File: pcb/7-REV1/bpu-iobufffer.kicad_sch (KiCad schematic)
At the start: 44 parts, among them J301 Conn_01x10, J302 Conn_01x09, U14 IP4220CZ6F, U15 IP4220CZ6F, U301 AiP74LVC1T45GC363.TR, U302 AiP74LVC1T45GC363.TR, U303 AiP74LVC1T45GC363.TR, U304 AiP74LVC1T45GC363.TR, U305 AiP74LVC1T45GC363.TR, U306 AiP74LVC1T45GC363.TR, U307 AiP74LVC1T45GC363.TR, U308 AiP74LVC1T45GC363.TR

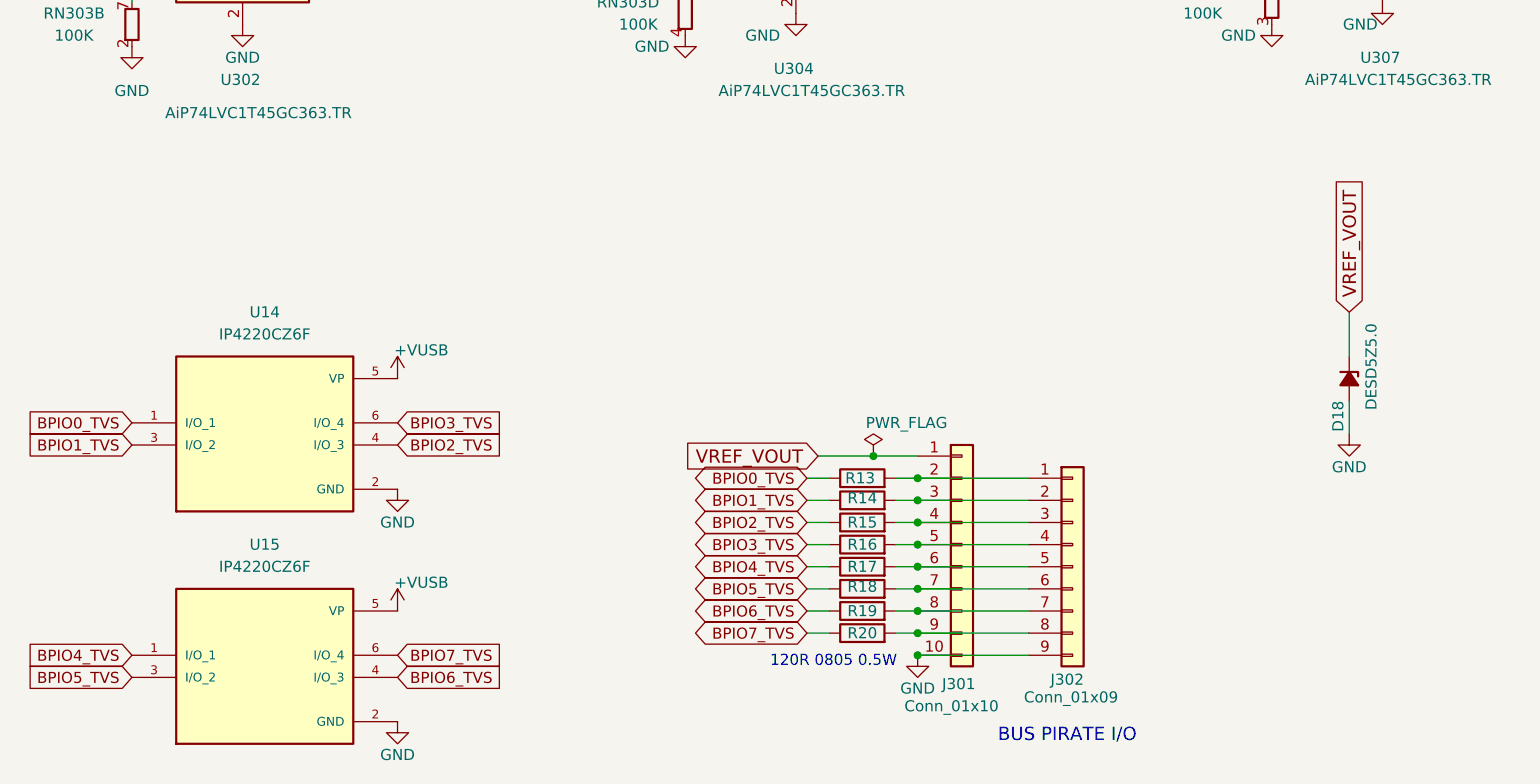
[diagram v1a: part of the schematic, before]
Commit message: adapt the IO-port protection
- move to the bpu-iobuffer sheet, remove duplicate on VOUT-protection
- use SP3002-04JTG in SOT363 instead of the larger IP4220CZ6F
- add datasheet, resistor wattage to part fields
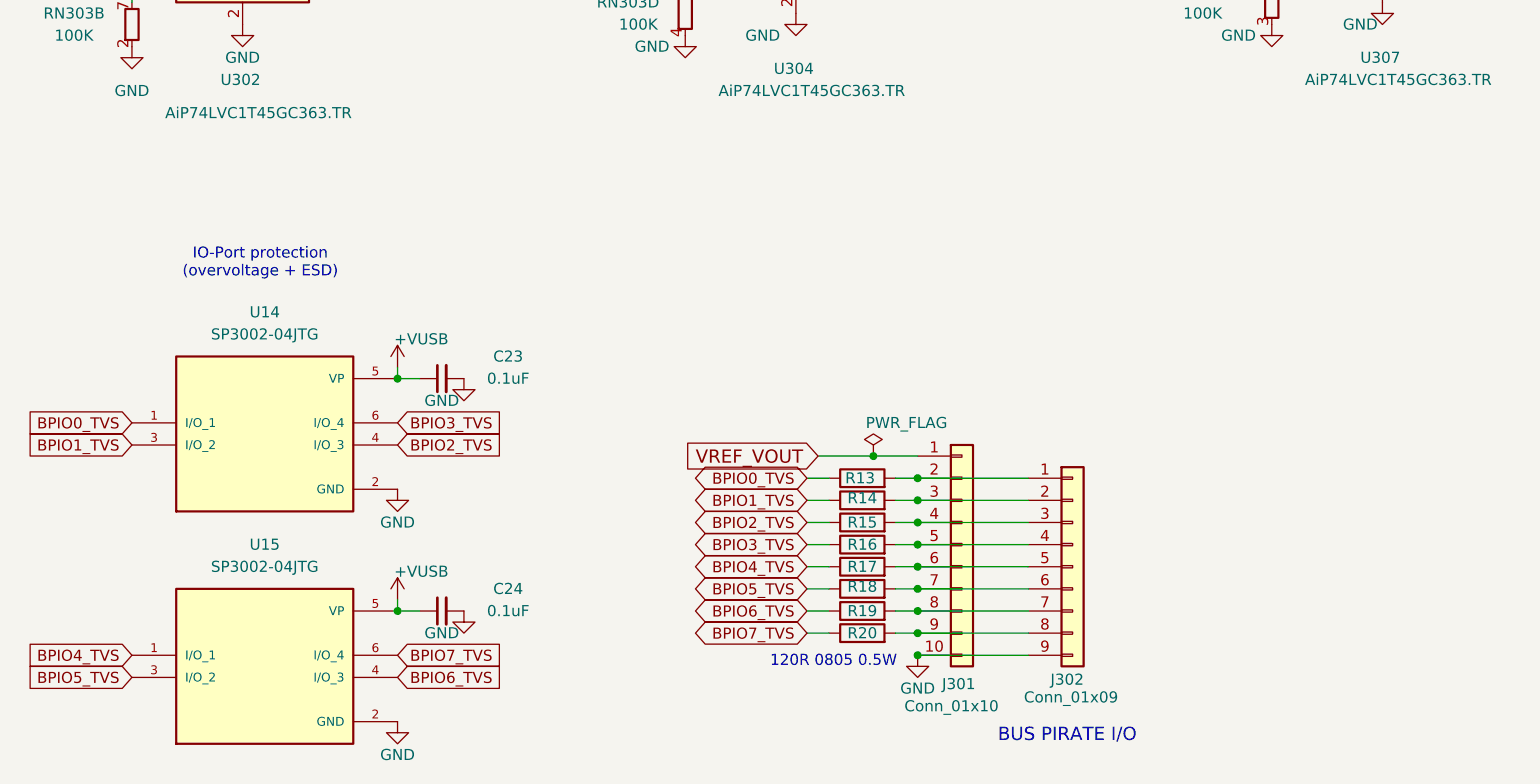
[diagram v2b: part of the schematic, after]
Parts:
- removed D18: DESD5Z5.0, Diode_SMD:D_SOD-523, symbol Device:D_Zener_Small_Filled
- added C23, C24: 0.1uF, Capacitor_SMD:C_0402_1005Metric, symbol Device:C_Small
- R13, R14, R15, R16, R17, R18, R19, R20: value 120R -> 120R 0.5W
- U14, U15: value IP4220CZ6F -> SP3002-04JTG; footprint library:SOT95P275X110-6N -> Package_TO_SOT_SMD:SOT-363_SC-70-6; Availability In Stock -> (none); Check_prices https://www.snapeda.com/parts/IP4220CZ6F/Nexperia/view-part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 -> (none); Description_1 - Clamp - Ipp Tvs Diode Surface Mount 6-TSOP -> (none); MANUFACTURER Nexperia -> Littelfuse; MAXIMUM_PACKAGE_HEIGHT 1.1 mm -> (none); MF Nexperia USA Inc. -> (none); MP IP4220CZ6F -> (none); PARTREV 5 -> (none); Package SOT-457 Nexperia USA -> (none); Price None -> (none); STANDARD IPC 7351B -> (none); SnapEDA_Link https://www.snapeda.com/parts/IP4220CZ6F/Nexperia/view-part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 -> (none)
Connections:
- net +VUSB: now also C23.1, C24.1
- net GND: now also C23.2, C24.2
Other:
- note added: "IO-Port protection (overvoltage + ESD)"

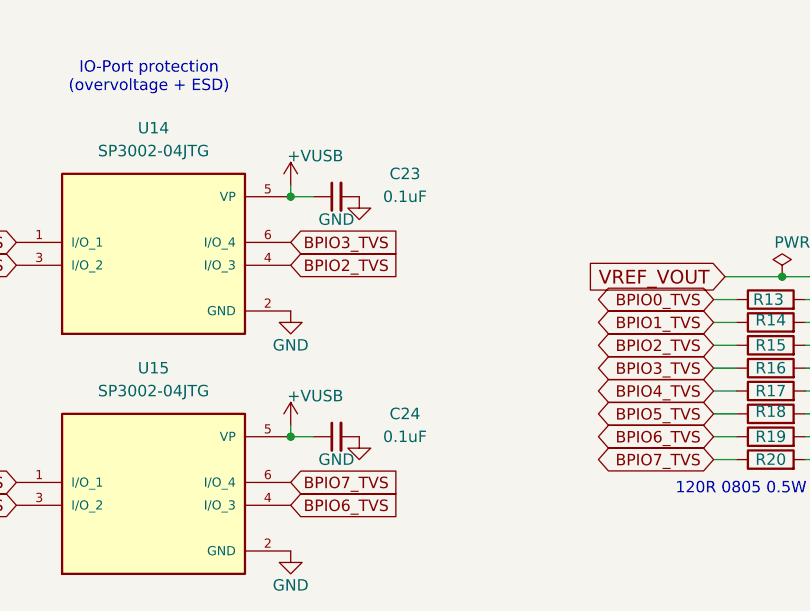
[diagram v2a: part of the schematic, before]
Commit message: change the decoupling caps for the SP3002-04JTG TVS diodes to 4.7µF
Lower impedanced decoupling, can absorb more energy fast
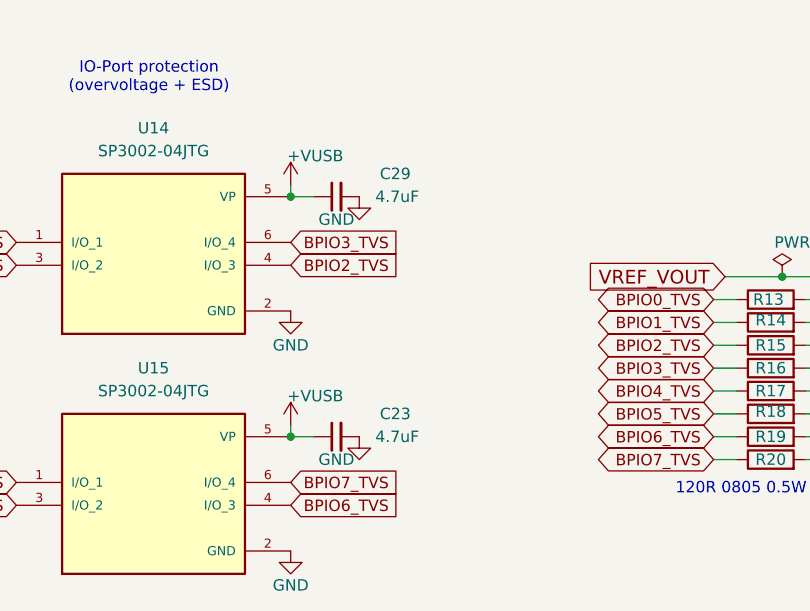
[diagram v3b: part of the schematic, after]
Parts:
- removed C24: 0.1uF, Capacitor_SMD:C_0402_1005Metric, symbol Device:C_Small
- added C29: 4.7uF, Capacitor_SMD:C_0402_1005Metric, symbol Device:C_Small
- C23: value 0.1uF -> 4.7uF; RMB 0.00628 -> 0.037726
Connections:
- net +VUSB: now also C29.1
- net GND: now also C29.2
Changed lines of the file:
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@@
 	(symbol
 		(lib_id "Device:C_Small")
-		(at 72.39 175.26 90)
-		(unit 1)
-		(exclude_from_sim no)
-		(in_bom yes)
-		(on_board yes)
-		(dnp no)
-		(property "Reference" "C24"
-			(at 80.01 172.72 90)
-			(effects
-				(font
-					(size 1.27 1.27)
-				)
-			)
-		)
-		(property "Value" "0.1uF"
-			(at 80.01 175.26 90)
-			(effects
-				(font
-					(size 1.27 1.27)
-				)
+		(at 72.39 148.59 90)
+		(unit 1)
+		(exclude_from_sim no)
+		(in_bom yes)
+		(on_board yes)
+		(dnp no)
+		(property "Reference" "C29"
+			(at 77.216 146.05 90)
+			(effects
+				(font
+					(size 1.27 1.27)
+				)
+				(justify right)
+			)
+		)
+		(property "Value" "4.7uF"
+			(at 76.708 148.59 90)
+			(effects
+				(font
+					(size 1.27 1.27)
+				)
+				(justify right)
 			)
 		)
 		(property "Footprint" "Capacitor_SMD:C_0402_1005Metric"
-			(at 72.39 175.26 0)
+			(at 72.39 148.59 0)
 			(effects
 				(font
@@
 		)
 		(property "Datasheet" "~"
-			(at 72.39 175.26 0)
+			(at 72.39 148.59 0)
 			(effects
 				(font
@@
 		)
 		(property "Description" ""
-			(at 72.39 175.26 0)
-			(effects
-				(font
-					(size 1.27 1.27)
-				)
-				(hide yes)
-			)
-		)
-		(property "RMB" "0.00628"
-			(at 72.39 175.26 0)
+			(at 72.39 148.59 0)
+			(effects
+				(font
+					(size 1.27 1.27)
+				)
+				(hide yes)
+			)
+		)
+		(property "RMB" "0.037726"
+			(at 72.39 148.59 0)
 			(effects
 				(font
@@
 		)
 		(property "Supplier" "https://item.szlcsc.com/1877.html"
-			(at 72.39 175.26 0)
+			(at 72.39 148.59 0)
 			(effects
 				(font
@@
 			(project "7-REV1"
 				(path "/1f56410a-eaac-4444-b0f7-cfd3531e22ac/00000000-0000-0000-0000-00005f344f30"
-					(reference "C24")
+					(reference "C29")
 					(unit 1)
 				)
@@
 	)
 	(symbol
+		(lib_id "Device:C_Small")
+		(at 72.39 175.26 90)
+		(unit 1)
+		(exclude_from_sim no)
+		(in_bom yes)
+		(on_board yes)
+		(dnp no)
+		(property "Reference" "C23"
+			(at 77.216 172.72 90)
+			(effects
+				(font
+					(size 1.27 1.27)
+				)
+				(justify right)
+			)
+		)
+		(property "Value" "4.7uF"
+			(at 76.708 175.26 90)
+			(effects
+				(font
+					(size 1.27 1.27)
+				)
+				(justify right)
+			)
+		)
+		(property "Footprint" "Capacitor_SMD:C_0402_1005Metric"
+			(at 72.39 175.26 0)
+			(effects
+				(font
+					(size 1.27 1.27)
+				)
+				(hide yes)
+			)
+		)
+		(property "Datasheet" "~"
+			(at 72.39 175.26 0)
+			(effects
+				(font
+					(size 1.27 1.27)
+				)
+				(hide yes)
+			)
+		)
+		(property "Description" ""
+			(at 72.39 175.26 0)
+			(effects
+				(font
+					(size 1.27 1.27)
+				)
+				(hide yes)
+			)
+		)
+		(property "RMB" "0.037726"
+			(at 72.39 175.26 0)
+			(effects
+				(font
+					(size 1.27 1.27)
+				)
+				(hide yes)
+			)
+		)
+		(property "Supplier" "https://item.szlcsc.com/1877.html"
+			(at 72.39 175.26 0)
+			(effects
+				(font
+					(size 1.27 1.27)
+				)
+				(hide yes)
+			)
+		)
+		(pin "1"
+		)
+		(pin "2"
+		)
+		(instances
+			(project "7-REV1"
+				(path "/1f56410a-eaac-4444-b0f7-cfd3531e22ac/00000000-0000-0000-0000-00005f344f30"
+					(reference "C23")
+					(unit 1)
+				)
+			)
+		)
+	)
+	(symbol
 		(lib_id "IP4220CZ6F:IP4220CZ6F")
 		(at 52.07 153.67 0)
@@
 					(unit 1)
 				)
-			)
-		)
-	)
-	(symbol
-		(lib_id "Device:C_Small")
-		(at 72.39 148.59 90)
-		(unit 1)
-		(exclude_from_sim no)
-		(in_bom yes)
-		(on_board yes)
-		(dnp no)
-		(property "Reference" "C23"
-			(at 80.01 146.05 90)
-			(effects
-				(font
-					(size 1.27 1.27)
-				)
-			)
-		)
-		(property "Value" "0.1uF"
-			(at 80.01 148.59 90)
-			(effects
-				(font
-					(size 1.27 1.27)
-				)
-			)
-		)
-		(property "Footprint" "Capacitor_SMD:C_0402_1005Metric"
-			(at 72.39 148.59 0)
-			(effects
-				(font
-					(size 1.27 1.27)
-				)
-				(hide yes)
-			)
-		)
-		(property "Datasheet" "~"
-			(at 72.39 148.59 0)
-			(effects
-				(font
-					(size 1.27 1.27)
-				)
-				(hide yes)
-			)
-		)
-		(property "Description" ""
-			(at 72.39 148.59 0)
-			(effects
-				(font
-					(size 1.27 1.27)
-				)
-				(hide yes)
-			)
-		)
-		(property "RMB" "0.00628"
-			(at 72.39 148.59 0)
-			(effects
-				(font
-					(size 1.27 1.27)
-				)
-				(hide yes)
-			)
-		)
-		(property "Supplier" "https://item.szlcsc.com/1877.html"
-			(at 72.39 148.59 0)
-			(effects
-				(font
-					(size 1.27 1.27)
-				)
-				(hide yes)
-			)
-		)
-		(pin "1"
-		)
-		(pin "2"
-		)
-		(instances
-			(project "7-REV1"
-				(path "/1f56410a-eaac-4444-b0f7-cfd3531e22ac/00000000-0000-0000-0000-00005f344f30"
-					(reference "C23")
-					(unit 1)
-				)

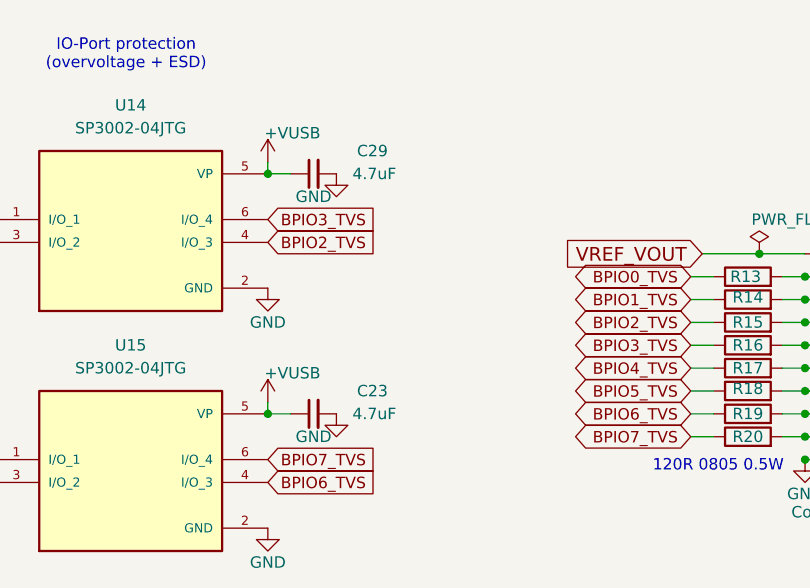
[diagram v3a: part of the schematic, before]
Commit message: BP7REV1 2.2uF, 4.7uF-> 10uF/6.3V CL05A106MQ5NUN. 520K->470K on reset/bootloader switch.
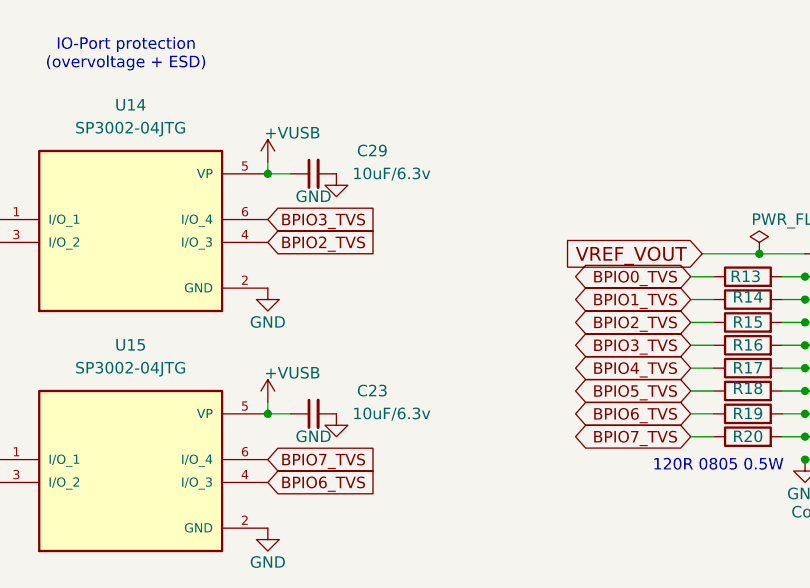
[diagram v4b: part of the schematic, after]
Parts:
- C23, C29: value 4.7uF -> 10uF/6.3v
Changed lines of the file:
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@@
 			)
 		)
-		(property "Value" "4.7uF"
+		(property "Value" "10uF/6.3v"
 			(at 76.708 148.59 90)
 			(effects
@@
 			)
 		)
-		(property "Description" ""
+		(property "Description" "CL05A106MQ5NUN"
 			(at 72.39 148.59 0)
 			(effects
@@
 			)
 		)
-		(property "Value" "4.7uF"
+		(property "Value" "10uF/6.3v"
 			(at 76.708 175.26 90)
 			(effects
@@
 			)
 		)
-		(property "Description" ""
+		(property "Description" "CL05A106MQ5NUN"
 			(at 72.39 175.26 0)
 			(effects

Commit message: specify part numbers and manufacturers in more detail - 10µF / 0805 caps - 2N7002KT fets
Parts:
- C23, C29: MANUFACTURER (none) -> Samsung
